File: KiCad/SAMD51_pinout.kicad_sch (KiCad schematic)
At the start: 10 parts, among them U4 SAMD51

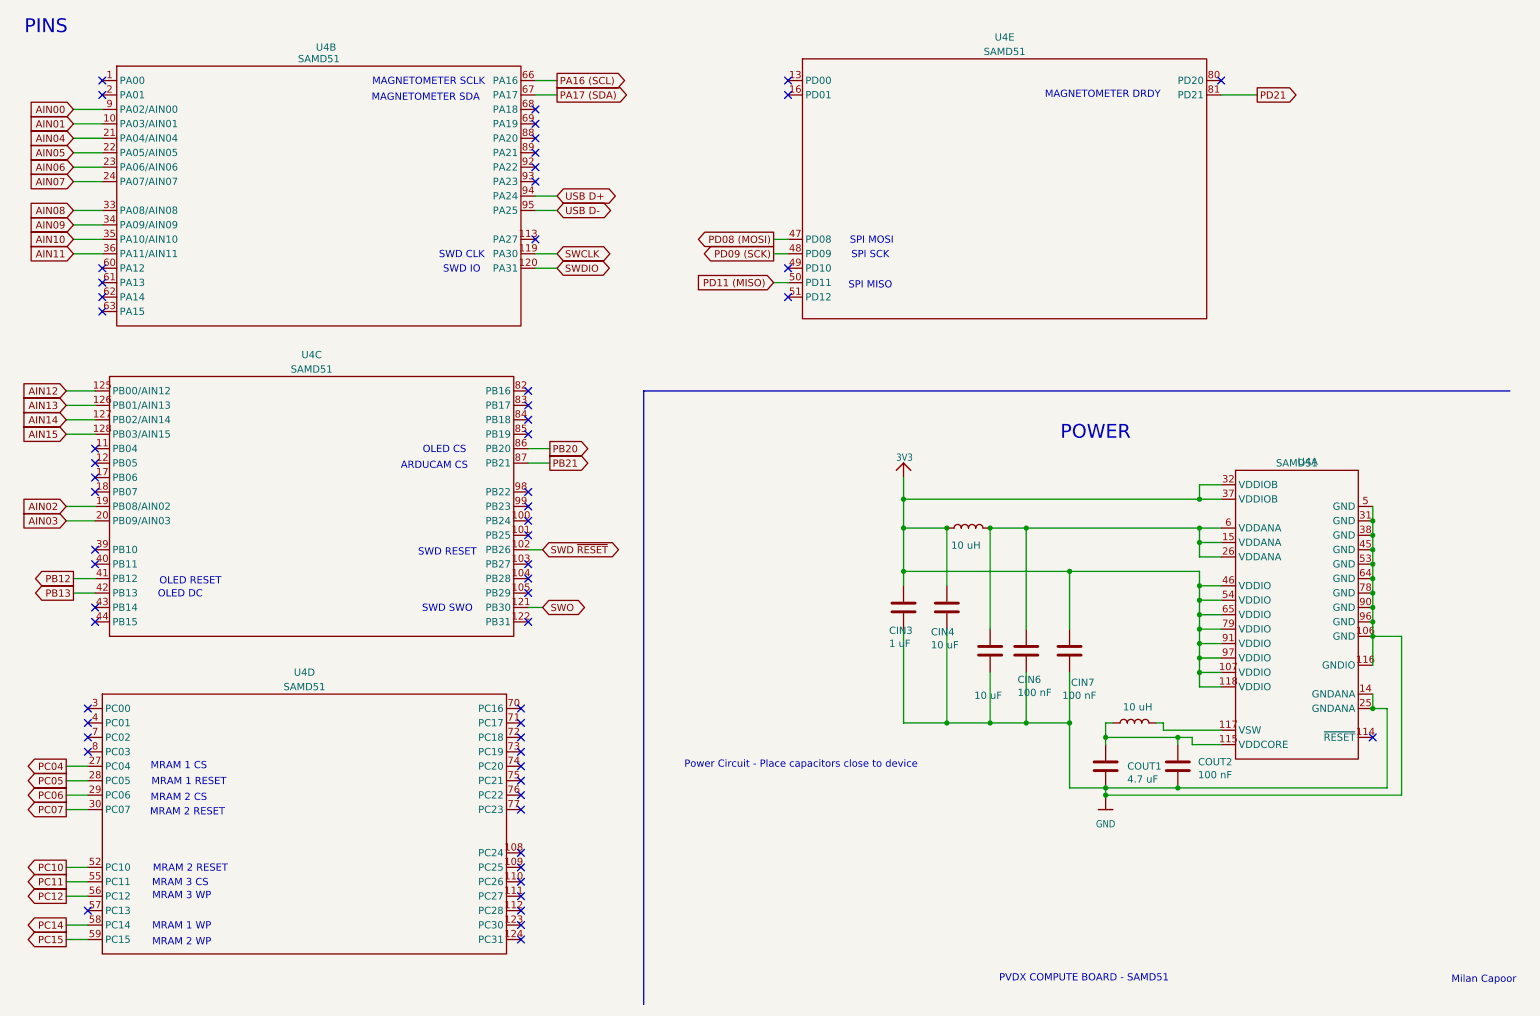
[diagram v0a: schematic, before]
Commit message: updated pins to match new spec and exposed all pins
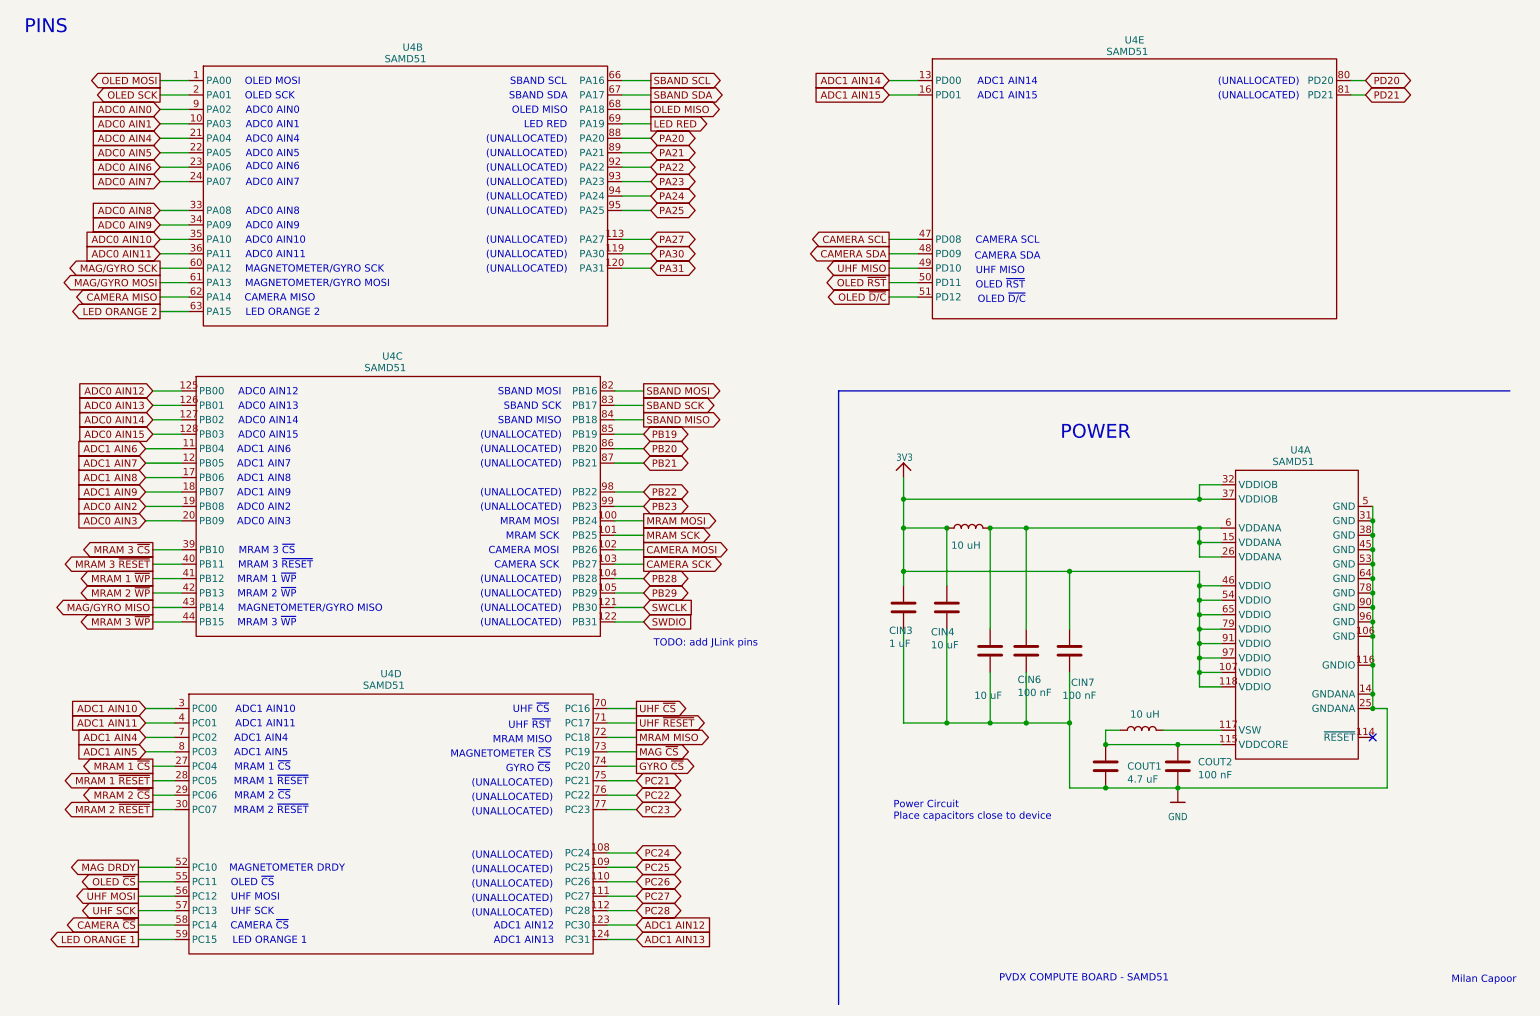
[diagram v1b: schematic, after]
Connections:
- net SWO is gone; now on net SWCLK: U4.121 (PB30)
- net SWCLK: no longer U4.119 (PA30)
- net SWDIO: now also U4.122 (PB31); no longer U4.120 (PA31)
- net OLED MOSI: now reaches U4.1 (PA00)
- net PA27: now reaches U4.113 (PA27)
- net OLED SCK: now reaches U4.2 (PA01)
- net MAG/GYRO SCK: now reaches U4.60 (PA12)
- net MAG/GYRO MOSI: now reaches U4.61 (PA13)
- net CAMERA MISO: now reaches U4.62 (PA14)
- net LED ORANGE 2: now reaches U4.63 (PA15)
- net OLED MISO: now reaches U4.68 (PA18)
- net LED RED: now reaches U4.69 (PA19)
- net PA20: now reaches U4.88 (PA20)
- net PA21: now reaches U4.89 (PA21)
- net PA22: now reaches U4.92 (PA22)
- net PA23: now reaches U4.93 (PA23)
- net PC24: now reaches U4.108 (PC24)
- net PC25: now reaches U4.109 (PC25)
- net PC26: now reaches U4.110 (PC26)
- net PC27: now reaches U4.111 (PC27)
- net PC28: now reaches U4.112 (PC28)
- net ADC1 AIN12: now reaches U4.123 (PC30)
- net ADC1 AIN13: now reaches U4.124 (PC31)
- net ADC1 AIN10: now reaches U4.3 (PC00)
- net ADC1 AIN11: now reaches U4.4 (PC01)
- net UHF SCK: now reaches U4.57 (PC13)
- net ADC1 AIN4: now reaches U4.7 (PC02)
- net UHF ~{CS}: now reaches U4.70 (PC16)
- net UHF ~{RESET}: now reaches U4.71 (PC17)
- net MRAM MISO: now reaches U4.72 (PC18)
- net MAG ~{CS}: now reaches U4.73 (PC19)
- net GYRO ~{CS}: now reaches U4.74 (PC20)
- net PC21: now reaches U4.75 (PC21)
- net PC22: now reaches U4.76 (PC22)
- net PC23: now reaches U4.77 (PC23)
- net ADC1 AIN5: now reaches U4.8 (PC03)
- net ADC1 AIN14: now reaches U4.13 (PD00)
- net ADC1 AIN15: now reaches U4.16 (PD01)
- net UHF MISO: now reaches U4.49 (PD10)
- net OLED ~{D/C}: now reaches U4.51 (PD12)
- net PD20: now reaches U4.80 (PD20)
- net MRAM MOSI: now reaches U4.100 (PB24)
- net MRAM SCK: now reaches U4.101 (PB25)
- net CAMERA SCK: now reaches U4.103 (PB27)
- net PB28: now reaches U4.104 (PB28)
- net PB29: now reaches U4.105 (PB29)
- net ADC1 AIN6: now reaches U4.11 (PB04)
- net ADC1 AIN7: now reaches U4.12 (PB05)
- net ADC1 AIN8: now reaches U4.17 (PB06)
- net ADC1 AIN9: now reaches U4.18 (PB07)
- net MRAM 3 ~{CS}: now reaches U4.39 (PB10)
- net MRAM 3 ~{RESET}: now reaches U4.40 (PB11)
- net MAG/GYRO MISO: now reaches U4.43 (PB14)
- net MRAM 3 ~{WP}: now reaches U4.44 (PB15)
- net SBAND MOSI: now reaches U4.82 (PB16)
- net SBAND SCK: now reaches U4.83 (PB17)
- net SBAND MISO: now reaches U4.84 (PB18)
- net PB19: now reaches U4.85 (PB19)
- net PB22: now reaches U4.98 (PB22)
- net PB23: now reaches U4.99 (PB23)
- net AIN00 renamed ADC0 AIN0
- net AIN01 renamed ADC0 AIN1
- net AIN02 renamed ADC0 AIN2
- net AIN03 renamed ADC0 AIN3
- net AIN04 renamed ADC0 AIN4
- net AIN05 renamed ADC0 AIN5
- net AIN06 renamed ADC0 AIN6
- net AIN07 renamed ADC0 AIN7
- net AIN08 renamed ADC0 AIN8
- net AIN09 renamed ADC0 AIN9
- net AIN10 renamed ADC0 AIN10
- net AIN11 renamed ADC0 AIN11
- net AIN12 renamed ADC0 AIN12
- net AIN13 renamed ADC0 AIN13
- net AIN14 renamed ADC0 AIN14
- net AIN15 renamed ADC0 AIN15
- net PA16 (SCL) renamed SBAND SCL
- net PA17 (SDA) renamed SBAND SDA
- net PB12 renamed MRAM 1 ~{WP}
- net PB13 renamed MRAM 2 ~{WP}
- net PC04 renamed MRAM 1 ~{CS}
- net PC05 renamed MRAM 1 ~{RESET}
- net PC06 renamed MRAM 2 ~{CS}
- net PC07 renamed MRAM 2 ~{RESET}
- net PC10 renamed MAG DRDY
- net PC11 renamed OLED ~{CS}
- net PC12 renamed UHF MOSI
- net PC14 renamed CAMERA ~{CS}
- net PC15 renamed LED ORANGE 1
- net PD08 (MOSI) renamed CAMERA SCL
- net PD09 (SCK) renamed CAMERA SDA
- net PD11 (MISO) renamed OLED ~{RST}
- net SWD ~{RESET} renamed CAMERA MOSI
- net USB D+ renamed PA24
- net USB D- renamed PA25
- new net PA30: U4.119 (PA30)
- new net PA31: U4.120 (PA31)
- no-connect marks 59 -> 1
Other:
- note added: "(UNALLOCATED)"
- note added: "ADC0 AIN0"
- note added: "ADC0 AIN1"
- note added: "ADC0 AIN10"
- note added: "ADC0 AIN11"
- note added: "ADC0 AIN12"
- note added: "ADC0 AIN13"
- note added: "ADC0 AIN14"
- note added: "ADC0 AIN15"
- note added: "ADC0 AIN2"
- note added: "ADC0 AIN3"
- note added: "ADC0 AIN4"
- note added: "ADC0 AIN5"
- note added: "ADC0 AIN6"
- note added: "ADC0 AIN7"
- note added: "ADC0 AIN8"
- note added: "ADC0 AIN9"
- note added: "ADC1 AIN10"
- note added: "ADC1 AIN11"
- note added: "ADC1 AIN12"
- note added: "ADC1 AIN13"
- note added: "ADC1 AIN14"
- note added: "ADC1 AIN15"
- note added: "ADC1 AIN4"
- note added: "ADC1 AIN5"
- note added: "ADC1 AIN6"
- note added: "ADC1 AIN7"
- note added: "ADC1 AIN8"
- note added: "ADC1 AIN9"
- note added: "CAMERA MISO"
- note added: "CAMERA MOSI"
- note added: "CAMERA SCK"
- note added: "CAMERA SCL"
- note added: "CAMERA SDA"
- note added: "CAMERA ~{CS}"
- note added: "GYRO ~{CS}"
- note added: "LED ORANGE 1"
- note added: "LED ORANGE 2"
- note added: "LED RED"
- note added: "MAGNETOMETER ~{CS}"
- note added: "MAGNETOMETER/GYRO MISO"
- note added: "MAGNETOMETER/GYRO MOSI"
- note added: "MAGNETOMETER/GYRO SCK"
- note added: "MRAM 1 ~{CS}"
- note added: "MRAM 1 ~{RESET}"
- note added: "MRAM 1 ~{WP}"
- note added: "MRAM 2 ~{CS}"
- note added: "MRAM 2 ~{RESET}"
- note added: "MRAM 2 ~{WP}"
- note added: "MRAM 3 ~{CS}"
- note added: "MRAM 3 ~{RESET}"
- note added: "MRAM 3 ~{WP}"
- note added: "MRAM MISO"
- note added: "MRAM MOSI"
- note added: "MRAM SCK"
- note added: "OLED MISO"
- note added: "OLED MOSI"
- note added: "OLED SCK"
- note added: "OLED ~{CS}"
- note added: "OLED ~{D/C}"
- note added: "OLED ~{RST}"
- note added: "Power Circuit Place capacitors close to device"
- note added: "SBAND MISO"
- note added: "SBAND MOSI"
- note added: "SBAND SCK"
- note added: "SBAND SCL"
- note added: "SBAND SDA"
- note added: "TODO: add JLink pins"
- note added: "UHF MISO"
- note added: "UHF MOSI"
- note added: "UHF SCK"
- note added: "UHF ~{CS}"
- note added: "UHF ~{RST}"
- note removed: "ARDUCAM CS"
- note removed: "MAGNETOMETER SCLK"
- note removed: "MAGNETOMETER SDA"
- note removed: "MRAM 1 CS"
- note removed: "MRAM 1 RESET"
- note removed: "MRAM 1 WP"
- note removed: "MRAM 2 CS"
- note removed: "MRAM 2 RESET"
- note removed: "MRAM 2 WP"
- note removed: "MRAM 3 CS"
- note removed: "MRAM 3 WP"
- note removed: "OLED CS"
- note removed: "OLED DC"
- note removed: "OLED RESET"
- note removed: "Power Circuit - Place capacitors close to device"
- note removed: "SPI MISO"
- note removed: "SPI MOSI"
- note removed: "SPI SCK"
- note removed: "SWD CLK"
- note removed: "SWD IO"
- note removed: "SWD RESET"
- note removed: "SWD SWO"
- moved on the sheet: U4B, U4C, U4D, U4E
